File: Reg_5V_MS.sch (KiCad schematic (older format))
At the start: 15 parts, among them U10 TPS53319

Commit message: fixed some footprints, should now be correct and complete
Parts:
- C10: footprint Capacitors_SMD:C_1210_HandSoldering -> Capacitors_SMD:C_1210
- C11, C12: footprint Capacitors_SMD:C_0603_HandSoldering -> Capacitors_SMD:C_0603
- C13, C14, C15: footprint Capacitors_SMD:C_0805_HandSoldering -> Capacitors_SMD:C_0805
- C16: footprint Capacitors_SMD:C_1206_HandSoldering -> Capacitors_SMD:C_1206
- L10: footprint (none) -> hedgehog_footprints:XAL60xx
- R10, R11, R12, R13, R14, R15: footprint Resistors_SMD:R_0402 -> Resistors_SMD:R_0603
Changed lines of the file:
@@
 LIBS:switches
 LIBS:Hedgehog-cache
-EELAYER 25 0
+EELAYER 26 0
 EELAYER END
 $Descr A4 11693 8268
@@
 F 0 "C10" H 3900 3850 50  0000 R CNN
 F 1 "22µ" H 3900 3925 50  0000 R CNN
-F 2 "Capacitors_SMD:C_1210_HandSoldering" H 3688 3750 50  0001 C CNN
+F 2 "Capacitors_SMD:C_1210" H 3688 3750 50  0001 C CNN
 F 3 "" H 3650 3900 50  0001 C CNN
 	1    3650 3900
@@
 F 0 "C11" H 3800 3850 50  0000 R CNN
 F 1 "4µ7" H 3800 3925 50  0000 R CNN
-F 2 "Capacitors_SMD:C_0603_HandSoldering" H 3938 3750 50  0001 C CNN
+F 2 "Capacitors_SMD:C_0603" H 3938 3750 50  0001 C CNN
 F 3 "" H 3900 3900 50  0001 C CNN
 	1    3900 3900
@@
 F 0 "C13" V 6800 3700 50  0000 C CNN
 F 1 "100n" V 6725 3700 50  0000 C CNN
-F 2 "Capacitors_SMD:C_0805_HandSoldering" H 6638 3550 50  0001 C CNN
+F 2 "Capacitors_SMD:C_0805" H 6638 3550 50  0001 C CNN
 F 3 "" H 6600 3700 50  0001 C CNN
 	1    6600 3700
@@
 F 0 "C14" H 7415 3596 50  0000 L CNN
 F 1 "1n" H 7425 3525 50  0000 L CNN
-F 2 "Capacitors_SMD:C_0805_HandSoldering" H 7338 3400 50  0001 C CNN
+F 2 "Capacitors_SMD:C_0805" H 7338 3400 50  0001 C CNN
 F 3 "" H 7300 3550 50  0001 C CNN
 	1    7300 3550
@@
 F 0 "C15" V 7700 3250 50  0000 C CNN
 F 1 "100n" V 7625 3250 50  0000 C CNN
-F 2 "Capacitors_SMD:C_0805_HandSoldering" H 7538 3100 50  0001 C CNN
+F 2 "Capacitors_SMD:C_0805" H 7538 3100 50  0001 C CNN
 F 3 "" H 7500 3250 50  0001 C CNN
 	1    7500 3250
@@
 F 0 "C16" H 8285 3804 50  0000 R CNN
 F 1 "100µ" H 8285 3895 50  0000 R CNN
-F 2 "Capacitors_SMD:C_1206_HandSoldering" H 8438 3700 50  0001 C CNN
+F 2 "Capacitors_SMD:C_1206" H 8438 3700 50  0001 C CNN
 F 3 "" H 8400 3850 50  0001 C CNN
 	1    8400 3850
@@
 F 0 "R10" H 4200 4250 50  0000 L CNN
 F 1 "<50k" H 4150 4175 50  0000 L CNN
-F 2 "Resistors_SMD:R_0402" V 4330 4200 50  0001 C CNN
+F 2 "Resistors_SMD:R_0603" V 4330 4200 50  0001 C CNN
 F 3 "" H 4400 4200 50  0001 C CNN
 	1    4400 4200
@@
 F 0 "C12" H 5000 4150 50  0000 R CNN
 F 1 "1µ" H 4975 4225 50  0000 R CNN
-F 2 "Capacitors_SMD:C_0603_HandSoldering" H 4788 4050 50  0001 C CNN
+F 2 "Capacitors_SMD:C_0603" H 4788 4050 50  0001 C CNN
 F 3 "" H 4750 4200 50  0001 C CNN
 	1    4750 4200
@@
 F 0 "R11" H 5150 4725 50  0000 L CNN
 F 1 "154k" H 5150 4650 50  0000 L CNN
-F 2 "Resistors_SMD:R_0402" V 5030 4600 50  0001 C CNN
+F 2 "Resistors_SMD:R_0603" V 5030 4600 50  0001 C CNN
 F 3 "" H 5100 4600 50  0001 C CNN
 	1    5100 4600
@@
 F 0 "R12" H 6575 4650 50  0000 L CNN
 F 1 "100k" H 6570 4555 50  0000 L CNN
-F 2 "Resistors_SMD:R_0402" V 6430 4600 50  0001 C CNN
+F 2 "Resistors_SMD:R_0603" V 6430 4600 50  0001 C CNN
 F 3 "" H 6500 4600 50  0001 C CNN
 	1    6500 4600
@@
 F 0 "R13" V 6925 3250 50  0000 C CNN
 F 1 "1k82" V 7000 3250 50  0000 C CNN
-F 2 "Resistors_SMD:R_0402" V 7030 3250 50  0001 C CNN
+F 2 "Resistors_SMD:R_0603" V 7030 3250 50  0001 C CNN
 F 3 "" H 7100 3250 50  0001 C CNN
 	1    7100 3250
@@
 F 0 "R14" H 8020 3746 50  0000 L CNN
 F 1 "69.8k" H 8020 3655 50  0000 L CNN
-F 2 "Resistors_SMD:R_0402" V 7880 3700 50  0001 C CNN
+F 2 "Resistors_SMD:R_0603" V 7880 3700 50  0001 C CNN
 F 3 "" H 7950 3700 50  0001 C CNN
 	1    7950 3700
@@
 F 0 "R15" H 8020 4346 50  0000 L CNN
 F 1 "10k" H 8020 4255 50  0000 L CNN
-F 2 "Resistors_SMD:R_0402" V 7880 4300 50  0001 C CNN
+F 2 "Resistors_SMD:R_0603" V 7880 4300 50  0001 C CNN
 F 3 "" H 7950 4300 50  0001 C CNN
 	1    7950 4300
@@
 F 0 "L10" V 7450 3000 50  0000 C CNN
 F 1 "2µ2" V 7375 3000 50  0000 C CNN
-F 2 "" H 7300 3000 50  0001 C CNN
+F 2 "hedgehog_footprints:XAL60xx" H 7300 3000 50  0001 C CNN
 F 3 "" H 7300 3000 50  0001 C CNN
 	1    7300 3000

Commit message: changed L and D of RPi 5V reg, all components on one side, everything routed, silkscreen unfinished
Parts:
- C13, C14, C15: footprint Capacitors_SMD:C_0805 -> Capacitors_SMD:C_0603
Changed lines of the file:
@@
 F 0 "C13" V 6800 3700 50  0000 C CNN
 F 1 "100n" V 6725 3700 50  0000 C CNN
-F 2 "Capacitors_SMD:C_0805" H 6638 3550 50  0001 C CNN
+F 2 "Capacitors_SMD:C_0603" H 6638 3550 50  0001 C CNN
 F 3 "" H 6600 3700 50  0001 C CNN
 	1    6600 3700
@@
 F 0 "C14" H 7415 3596 50  0000 L CNN
 F 1 "1n" H 7425 3525 50  0000 L CNN
-F 2 "Capacitors_SMD:C_0805" H 7338 3400 50  0001 C CNN
+F 2 "Capacitors_SMD:C_0603" H 7338 3400 50  0001 C CNN
 F 3 "" H 7300 3550 50  0001 C CNN
 	1    7300 3550
@@
 F 0 "C15" V 7700 3250 50  0000 C CNN
 F 1 "100n" V 7625 3250 50  0000 C CNN
-F 2 "Capacitors_SMD:C_0805" H 7538 3100 50  0001 C CNN
+F 2 "Capacitors_SMD:C_0603" H 7538 3100 50  0001 C CNN
 F 3 "" H 7500 3250 50  0001 C CNN
 	1    7500 3250

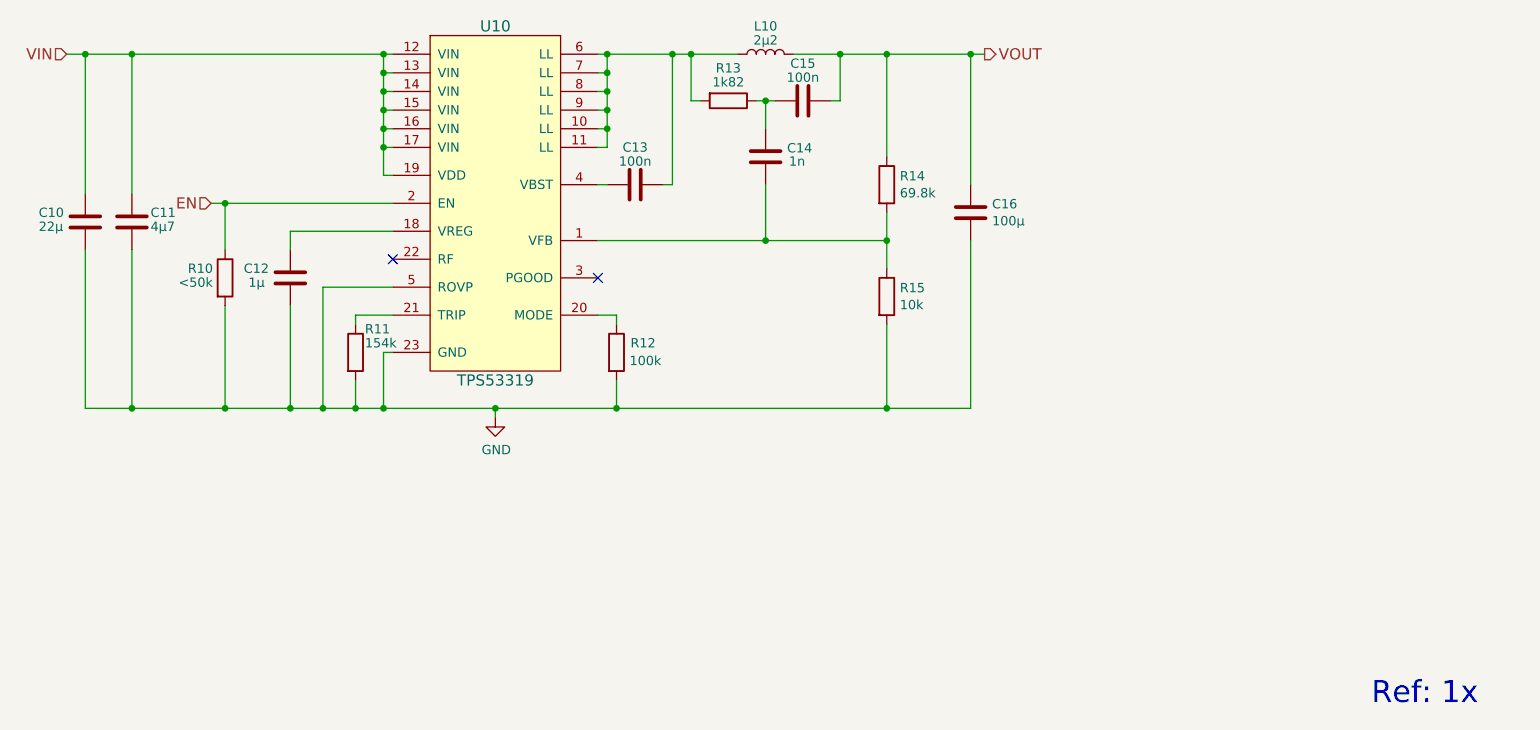
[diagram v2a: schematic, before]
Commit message: lots of changes: - incremented version number to 0.2 - all inputs are now analog, vbat for supply voltage monitoring - 6 servos - different 5v 10A regulator - changed input order - footprint fixes and cosmetic hanges - added fiducials - board size 0.5mm smaller - lots of other fixes and small changes
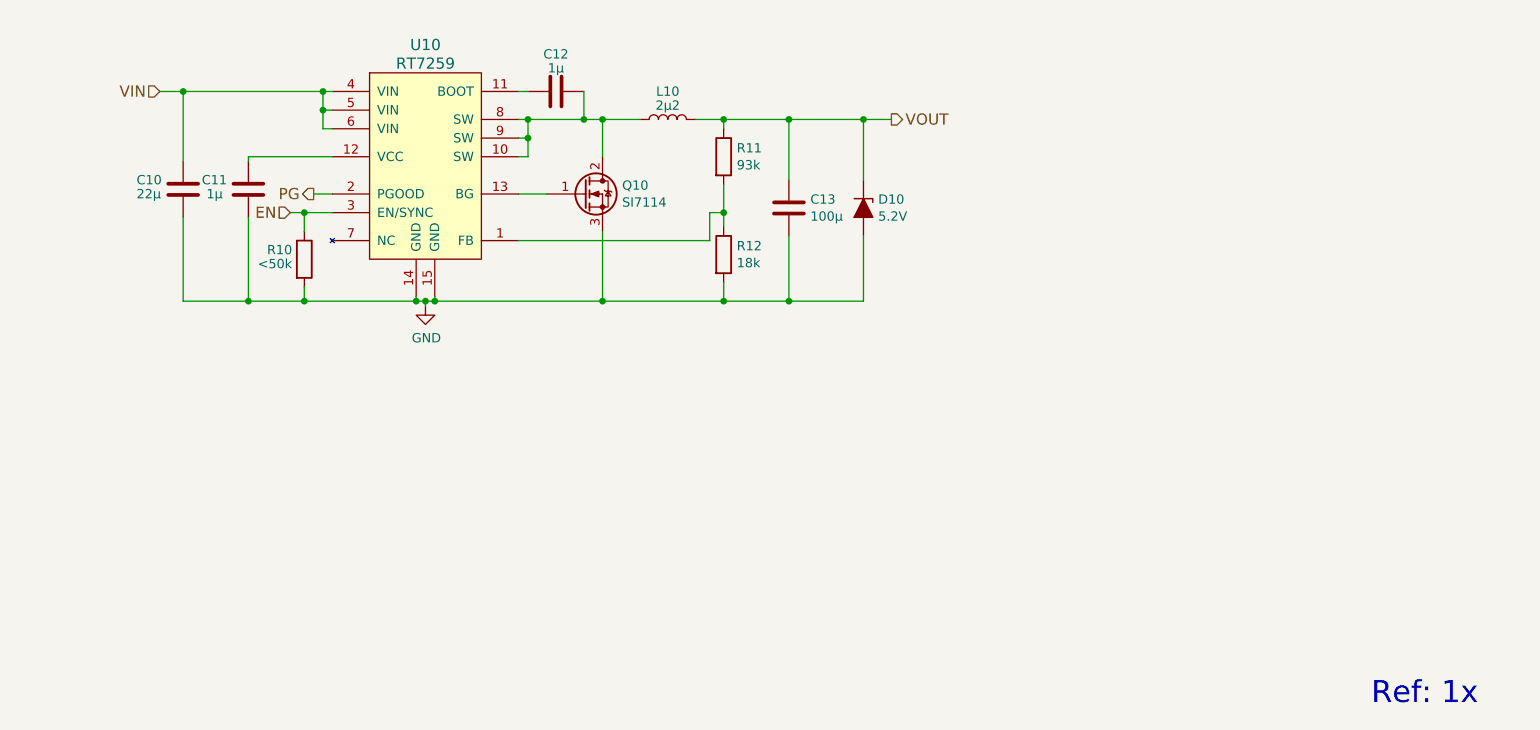
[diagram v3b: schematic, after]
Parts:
- removed C11: 4µ7, Capacitors_SMD:C_0603, symbol C
- removed C14: 1n, Capacitors_SMD:C_0603, symbol C
- removed C15: 100n, Capacitors_SMD:C_0603, symbol C
- removed R11: 154k, Resistors_SMD:R_0603, symbol R
- removed R12: 100k, Resistors_SMD:R_0603, symbol R
- removed R13: 1k82, Resistors_SMD:R_0603, symbol R
- removed U10: TPS53319, hedgehog_footprints:LSON-22, symbol TPS53319
- added D10: 5.2V, hedgehog_footprints:SOD123F, symbol D_Zener_ALT
- added Q10: SI7114, hedgehog_footprints:PowerPAK_1212-8, symbol Q_NMOS_GDS
- added U10: RT7259, hedgehog_footprints:DFN14_4x3, symbol RT7259
- C12: renamed from C13; value 100n -> 1µ
- R11: renamed from R14; value 69.8k -> 93k
- R12: renamed from R15; value 10k -> 18k
- renumbered C12 to C11, C16 to C13
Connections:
- net EN: now also U10.3 (EN/SYNC)
- net GND: now also D10.2 (A), Q10.3 (S), U10.14 (GND), U10.15 (GND)
- net VIN: now also U10.4 (VIN), U10.5 (VIN), U10.6 (VIN)
- net VOUT: now also D10.1 (K)
- net at R11.2, R12.1: now also U10.1 (FB)
- net at C12.2, L10.1: now also Q10.2 (D), U10.10 (SW), U10.8 (SW), U10.9 (SW)
- net at C11.2: now also U10.12 (VCC)
- net at C12.1: now also U10.11 (BOOT)
- new net: Q10.1 (G), U10.13 (BG)
- new net PG: U10.2 (PGOOD)
- no-connect marks 2 -> 0
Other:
- moved on the sheet: C10, C11, C12, C13, L10, R10, R11, R12

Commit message: component values changed documentation added
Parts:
- R10: value <50k -> 12k
- R11: value 93k -> 43k
- R12: value 18k -> 8k2
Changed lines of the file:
@@
 P 4825 4100
 F 0 "R10" H 4625 4150 50  0000 L CNN
-F 1 "<50k" H 4575 4075 50  0000 L CNN
+F 1 "12k" H 4625 4075 50  0000 L CNN
 F 2 "Resistors_SMD:R_0603" V 4755 4100 50  0001 C CNN
 F 3 "" H 4825 4100 50  0001 C CNN
@@
 P 7075 3550
 F 0 "R11" H 7145 3596 50  0000 L CNN
-F 1 "93k" H 7145 3505 50  0000 L CNN
+F 1 "43k" H 7145 3505 50  0000 L CNN
 F 2 "Resistors_SMD:R_0603" V 7005 3550 50  0001 C CNN
 F 3 "" H 7075 3550 50  0001 C CNN
@@
 P 7075 4075
 F 0 "R12" H 7145 4121 50  0000 L CNN
-F 1 "18k" H 7145 4030 50  0000 L CNN
+F 1 "8k2" H 7145 4030 50  0000 L CNN
 F 2 "Resistors_SMD:R_0603" V 7005 4075 50  0001 C CNN
 F 3 "" H 7075 4075 50  0001 C CNN

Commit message: upgraded project to new kicad symbol library format
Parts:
- C10, C11, C12, C13: symbol C -> Device:C
- D10: symbol D_Zener_ALT -> Device:D_Zener_ALT
- L10: symbol L -> Device:L
- Q10: symbol Q_NMOS_GDS -> Device:Q_NMOS_GDS
- R10, R11, R12: symbol R -> Device:R
- U10: symbol RT7259 -> hedgehog_symbols:RT7259
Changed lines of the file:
@@
-EESchema Schematic File Version 3
-LIBS:power
-LIBS:device
-LIBS:linear
-LIBS:regul
-LIBS:adc-dac
-LIBS:memory
-LIBS:xilinx
-LIBS:microcontrollers
-LIBS:dsp
-LIBS:microchip
-LIBS:analog_switches
-LIBS:motorola
-LIBS:texas
-LIBS:intel
-LIBS:audio
-LIBS:interface
-LIBS:digital-audio
-LIBS:philips
-LIBS:cypress
-LIBS:siliconi
-LIBS:opto
-LIBS:atmel
-LIBS:contrib
-LIBS:hedgehog_symbols
-LIBS:ac-dc
-LIBS:Altera
-LIBS:analog_devices
-LIBS:Battery_Management
-LIBS:bbd
-LIBS:bosch
-LIBS:brooktre
-LIBS:Connector
-LIBS:dc-dc
-LIBS:Diode
-LIBS:Display
-LIBS:driver_gate
-LIBS:DSP_Microchip_DSPIC33
-LIBS:elec-unifil
-LIBS:ESD_Protection
-LIBS:Espressif
-LIBS:FPGA_Actel
-LIBS:ftdi
-LIBS:gennum
-LIBS:Graphic
-LIBS:hc11
-LIBS:infineon
-LIBS:intersil
-LIBS:ir
-LIBS:Lattice
-LIBS:LED
-LIBS:LEM
-LIBS:Logic_74xgxx
-LIBS:Logic_74xx
-LIBS:Logic_CMOS_4000
-LIBS:Logic_CMOS_IEEE
-LIBS:logic_programmable
-LIBS:Logic_TTL_IEEE
-LIBS:maxim
-LIBS:MCU_Microchip_PIC10
-LIBS:MCU_Microchip_PIC12
-LIBS:MCU_Microchip_PIC16
-LIBS:MCU_Microchip_PIC18
-LIBS:MCU_Microchip_PIC24
-LIBS:MCU_Microchip_PIC32
-LIBS:MCU_NXP_Kinetis
-LIBS:MCU_NXP_LPC
-LIBS:MCU_NXP_S08
-LIBS:MCU_ST_STM8
-LIBS:MCU_Texas_MSP430
-LIBS:Mechanical
-LIBS:modules
-LIBS:Motor
-LIBS:motor_drivers
-LIBS:nordicsemi
-LIBS:nxp
-LIBS:onsemi
-LIBS:Oscillators
-LIBS:powerint
-LIBS:Power_Management
-LIBS:pspice
-LIBS:references
-LIBS:Relay
-LIBS:rfcom
-LIBS:RFSolutions
-LIBS:Sensor_Current
-LIBS:sensors
-LIBS:silabs
-LIBS:supertex
-LIBS:Switch
-LIBS:Transformer
-LIBS:Transistor
-LIBS:triac_thyristor
-LIBS:Valve
-LIBS:video
-LIBS:wiznet
-LIBS:Worldsemi
-LIBS:Xicor
-LIBS:zetex
-LIBS:Zilog
-LIBS:Hedgehog-cache
+EESchema Schematic File Version 4
 EELAYER 26 0
 EELAYER END
@@
 Ref: 1x
 $Comp
-L GND #PWR06
+L power:GND #PWR06
 U 1 1 5907589C
 P 5475 4350
@@
 $EndComp
 $Comp
-L C C10
+L Device:C C10
 U 1 1 5907CE70
 P 4175 3725
@@
 $EndComp
 $Comp
-L C C13
+L Device:C C13
 U 1 1 5907D42E
 P 7425 3825
@@
 $EndComp
 $Comp
-L R R10
+L Device:R R10
 U 1 1 5907D4C2
 P 4825 4100
@@
 $EndComp
 $Comp
-L C C11
+L Device:C C11
 U 1 1 5907D610
 P 4525 3725
@@
 $EndComp
 $Comp
-L R R11
+L Device:R R11
 U 1 1 5907D864
 P 7075 3550
@@
 $EndComp
 $Comp
-L R R12
+L Device:R R12
 U 1 1 5907D8F4
 P 7075 4075
@@
 $EndComp
 $Comp
-L L L10
+L Device:L L10
 U 1 1 5907D96F
 P 6775 3350
@@
 $EndComp
 $Comp
-L D_Zener_ALT D10
+L Device:D_Zener_ALT D10
 U 1 1 59EF3CBA
 P 7825 3825
@@
 $EndComp
 $Comp
-L C C12
+L Device:C C12
 U 1 1 5907D2A6
 P 6175 3200
@@
 Connection ~ 4925 3200
 $Comp
-L Q_NMOS_GDS Q10
+L Device:Q_NMOS_GDS Q10
 U 1 1 59F1426C
 P 6325 3750
@@
 Connection ~ 4175 3200
 $Comp
-L RT7259 U10
+L hedgehog_symbols:RT7259 U10
 U 1 1 59F17117
 P 5475 3600
